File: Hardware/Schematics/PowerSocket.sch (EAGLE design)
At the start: 72 parts, among them T1 BT138-H, T2 BT138-H, T3 BT138-H, T4 BT138-H, T5 BT138-H, T6 BT138-H

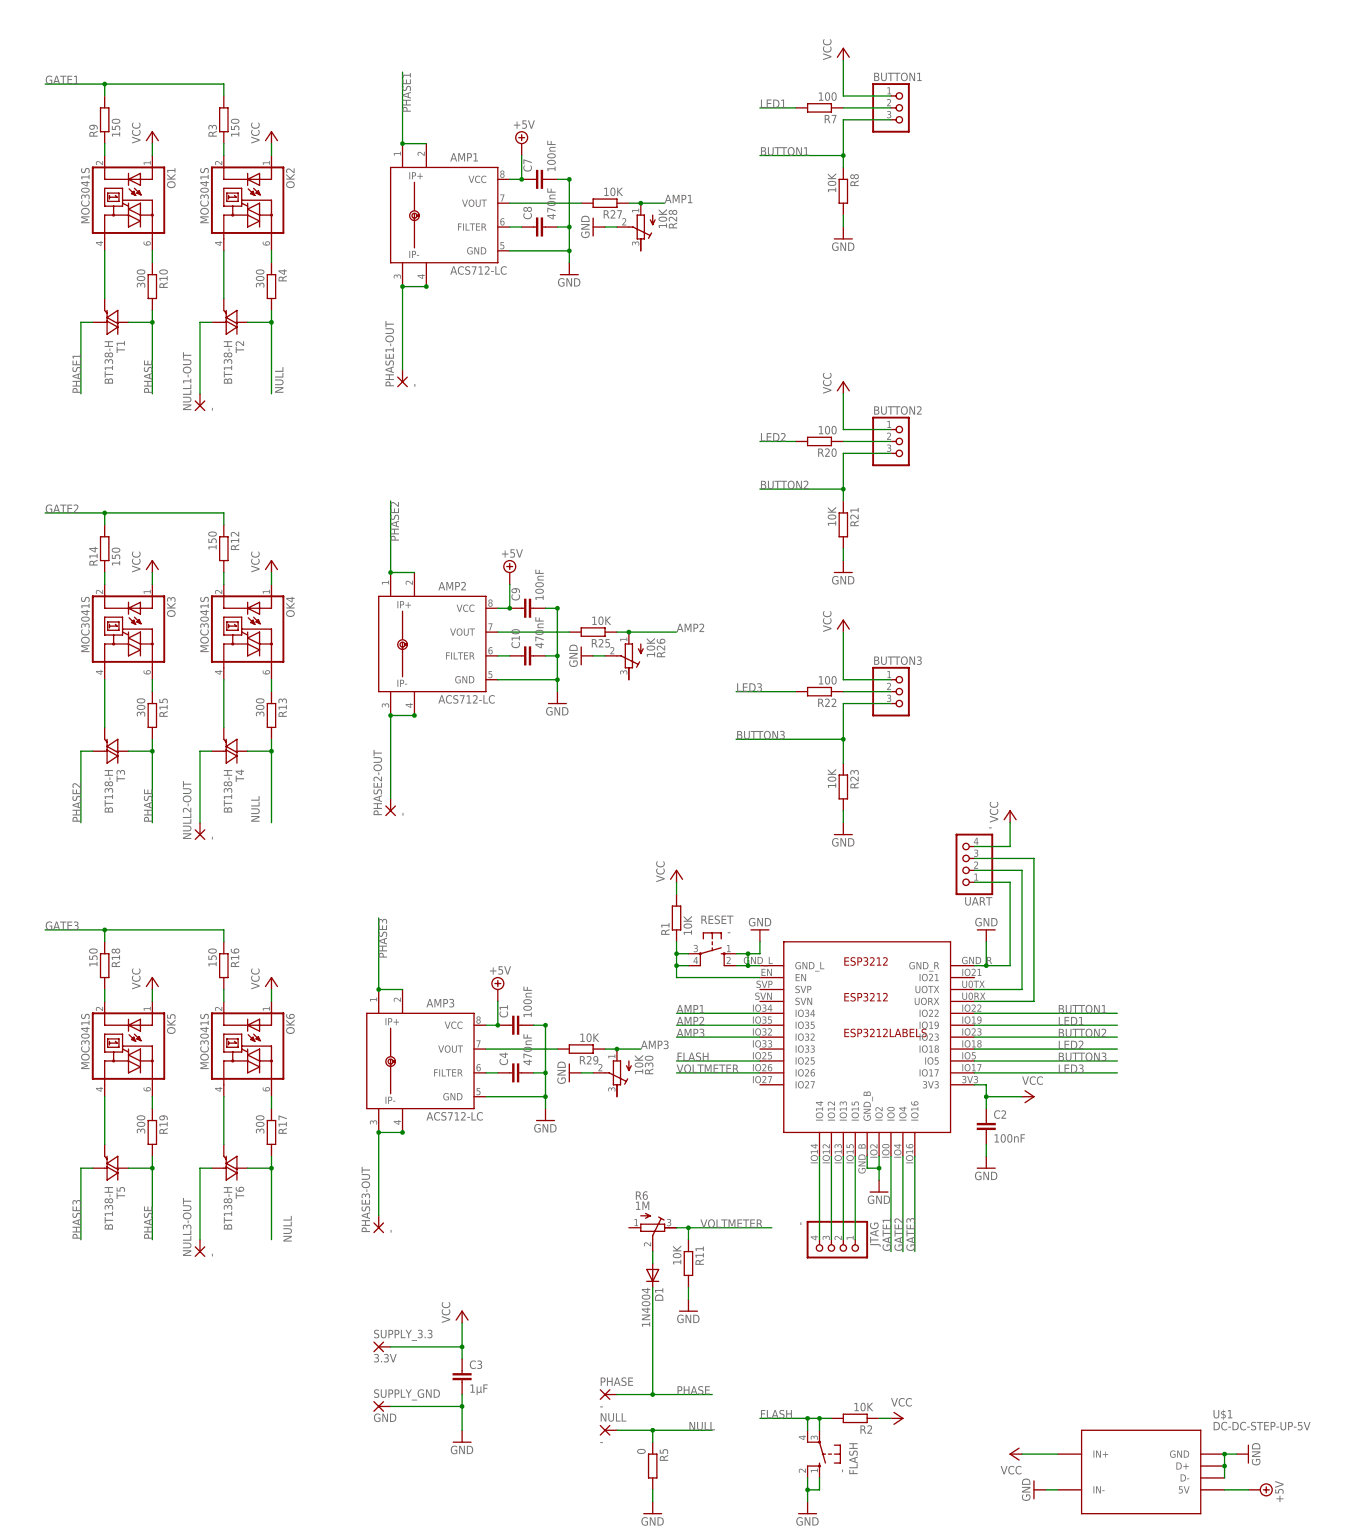
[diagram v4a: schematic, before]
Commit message: Replaced triacs with realys Replaced ESP3212 with ESP-12S
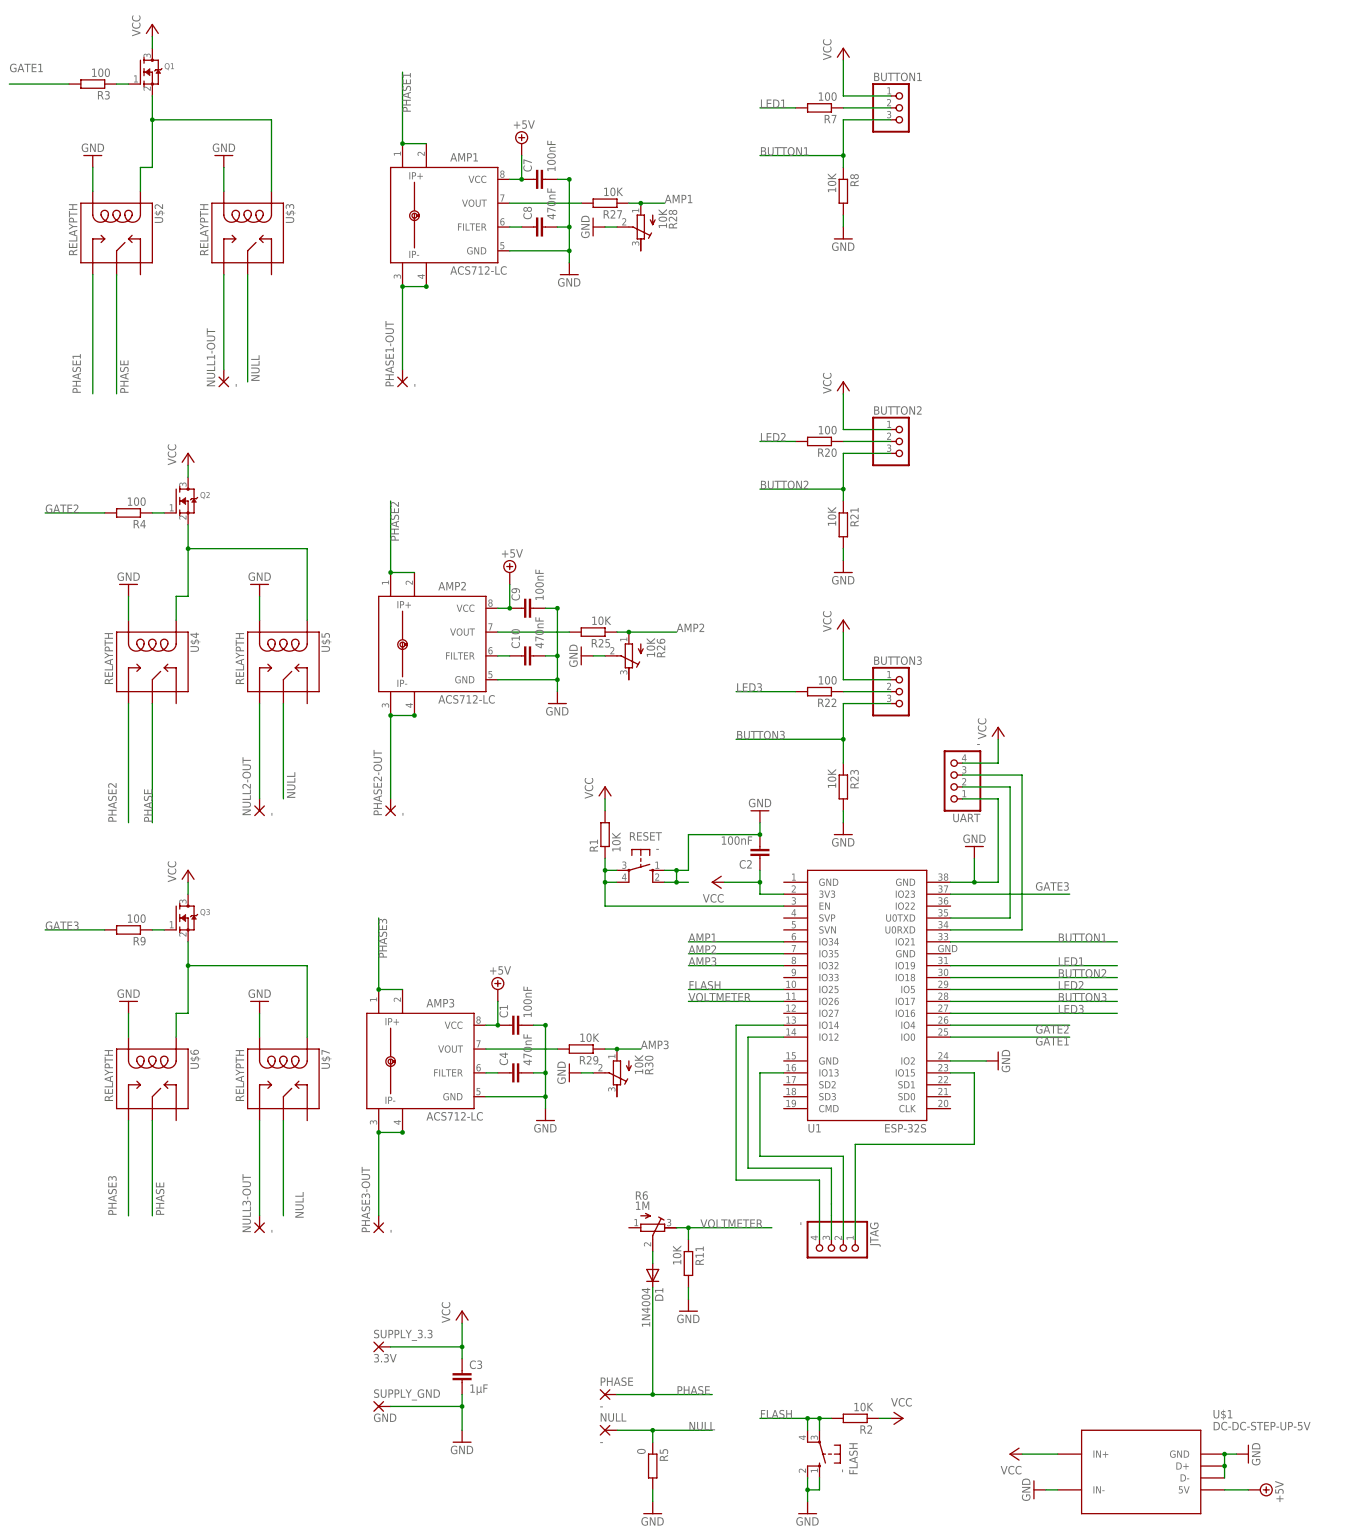
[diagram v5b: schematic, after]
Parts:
- removed ESP3212: ESP3212LABELS, esp3212-ptw:ESP3212LABELS
- removed OK1, OK2, OK3, OK4, OK5, OK6: MOC3041S, optocoupler:MOC3041S
- removed R10, R13, R15, R17, R19: 300, eagle-ltspice:RR2010
- removed R12, R14, R16, R18: 150, rcl:R-EU_R0805
- removed T1, T2, T3, T4, T5, T6: BT138-H, triac:BT138-H
- added Q1, Q2, Q3: (no value), adafruit:MOSFET-NREFLOW
- added U$2, U$3, U$4, U$5, U$6, U$7: RELAYPTH, SRD-05VDC-SL-C:RELAYPTH
- added U1: ESP-32S, esp32:ESP-32S
- R3, R9: value 150 -> 100
- R4: value 300 -> 100; device eagle-ltspice:RR2010 -> rcl:R-EU_R0805
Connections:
- removed net N$19: OK1.A1, T1.G
- removed net N$20: OK1.A2, R10.1
- removed net N$21: OK2.A2, R4.1
- removed net N$22: OK4.A1, T4.G
- removed net N$23: OK3.A2, R15.1
- removed net N$25: OK3.A1, T3.G
- removed net N$28: OK3.C, R14.1
- removed net N$29: OK4.C, R12.2
- removed net N$31: OK6.C, R16.2
- removed net N$33: OK6.A2, R17.1
- removed net N$34: OK6.A1, T6.G
- removed net N$35: OK5.A2, R19.1
- removed net N$36: OK5.A1, T5.G
- new net N$14: Q2.G, R4.1
- net AMP1: now also U1.IO34; no longer ESP3212.IO34
- net AMP2: now also U1.IO35; no longer ESP3212.IO35
- net AMP3: now also U1.IO32; no longer ESP3212.IO32
- net BUTTON1: now also U1.IO21; no longer ESP3212.IO22
- net BUTTON2: now also U1.IO18; no longer ESP3212.IO23
- net BUTTON3: now also U1.IO17; no longer ESP3212.IO5
- net FLASH: now also U1.IO25; no longer ESP3212.IO25
- net GATE1: now also U1.IO0; no longer ESP3212.IO0, R9.2
- net GATE2: now also R4.2, U1.IO4; no longer ESP3212.IO4, R12.1, R14.2
- net GATE3: now also R9.2, U1.IO23; no longer ESP3212.IO16, R16.1, R18.1
- net GND: now also U$2.COIL0, U$3.COIL0, U$4.COIL0, U$5.COIL0, U$6.COIL0, U$7.COIL0, U1.GND@3, U1.IO2; no longer ESP3212.GND_B, ESP3212.GND_L, ESP3212.GND_R, ESP3212.IO2
- net LED1: now also U1.IO19; no longer ESP3212.IO19
- net LED2: now also U1.IO5; no longer ESP3212.IO18
- net LED3: now also U1.IO16; no longer ESP3212.IO17
- net N$1: now also Q1.G, R3.1; no longer OK1.C, R9.1
- net N$15: now also Q2.S, U$4.COIL1, U$5.COIL1; no longer OK2.A1, T2.G
- net N$16: now also Q3.G, R9.1; no longer OK4.A2, R13.1
- net N$17: now also U$5.SWOPEN; no longer T4.A1
- net N$18: now also Q3.S, U$6.COIL1, U$7.COIL1; no longer OK5.C, R18.2
- net N$2: now also U1.IO15; no longer ESP3212.IO15
- net N$3: now also U1.IO13; no longer ESP3212.IO13
- net N$4: now also U1.IO12; no longer ESP3212.IO12
- net N$5: now also U1.IO14; no longer ESP3212.IO14
- net N$6: now also Q1.S, U$2.COIL1, U$3.COIL1; no longer OK2.C, R3.1
- net N$66: now also U1.EN; no longer ESP3212.EN
- net N$70: now also U1.U0TXD; no longer ESP3212.UOTX
- net N$77: now also U1.U0RXD; no longer ESP3212.UORX
- net N$8: now also U$3.SWOPEN; no longer T2.A1
- net NULL: now also U$3.SWCOMMON, U$5.SWCOMMON, U$7.SWCOMMON; no longer R13.2, R17.2, R4.2, T2.A2, T4.A2, T6.A2
- net NULL_: now also U$7.SWOPEN; no longer T6.A1
- net PHASE: now also U$2.SWCOMMON, U$4.SWCOMMON, U$6.SWCOMMON; no longer R10.2, R15.2, R19.2, T1.A2, T3.A2, T5.A2
- net PHASE1: now also U$2.SWOPEN; no longer T1.A1
- net PHASE2: now also U$4.SWOPEN; no longer T3.A1
- net PHASE3: now also U$6.SWOPEN; no longer T5.A1
- net VCC: now also Q1.D, Q2.D, Q3.D, U1.3V3; no longer ESP3212.3V3, OK1.A, OK2.A, OK3.A, OK4.A, OK5.A, OK6.A
- net VOLTMETER: now also U1.IO26; no longer ESP3212.IO26
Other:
- moved on the sheet: C2, NULL1-OUT, NULL2-OUT, NULL3-OUT, R1, R3, R4, R9, RESET, UART
